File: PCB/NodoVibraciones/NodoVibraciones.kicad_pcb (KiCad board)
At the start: 2 copper layers, 17 parts, among them J1 batería, J2 UART, J3 MPU6050, SW1 SW_Push, SW2 SW_Push, SW3 SW_Nidec_CAS-120A1, U1 ESP-07, U2 MPU-6050

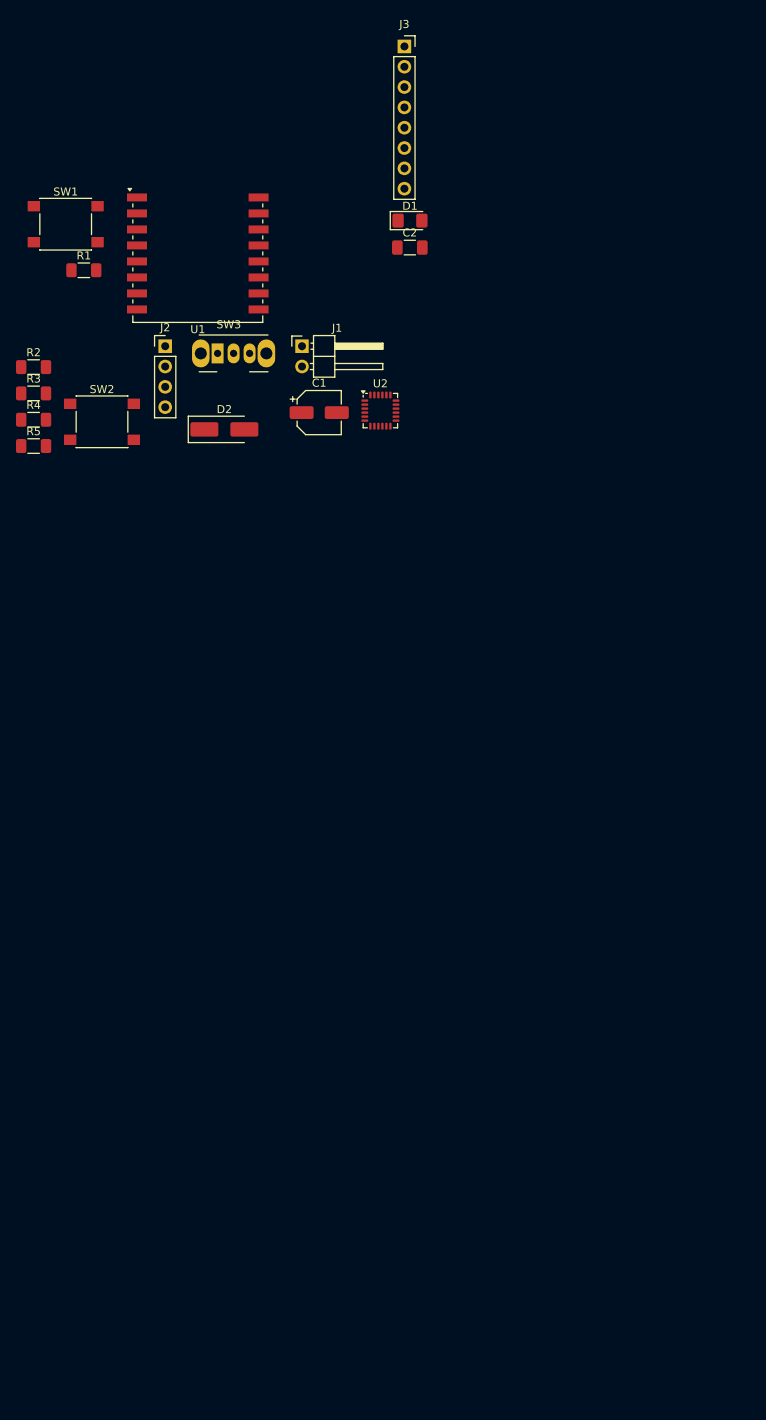
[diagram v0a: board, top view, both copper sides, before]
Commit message: Se creó PCB v0.0.1 de nodo VibraNet
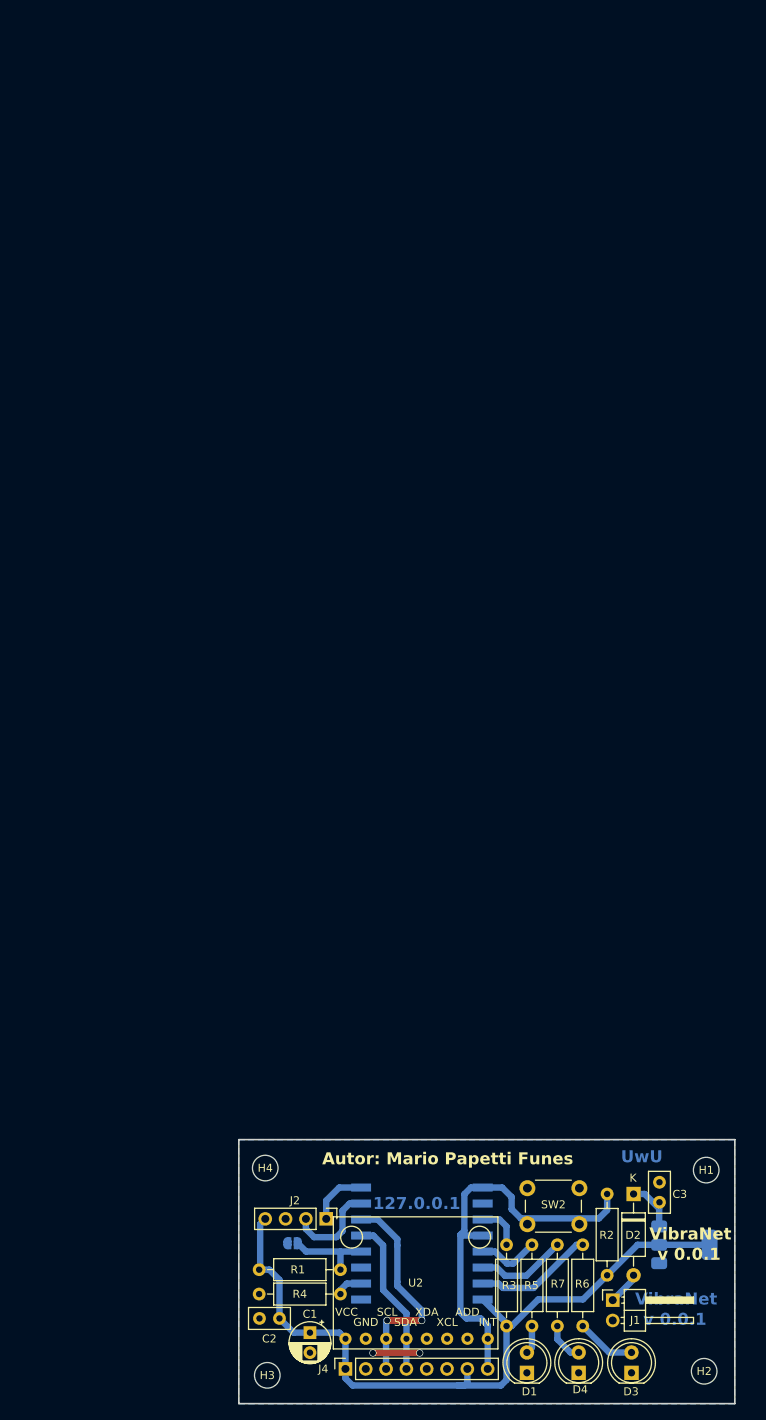
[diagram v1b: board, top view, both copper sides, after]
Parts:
- removed J3: MPU6050, Connector_PinSocket_2.54mm:PinSocket_1x08_P2.54mm_Vertical
- removed SW1: SW_Push, Button_Switch_SMD:SW_SPST_PTS645
- removed SW3: SW_Nidec_CAS-120A1, Button_Switch_THT:SW_Slide_SPDT_Angled_CK_OS102011MA1Q
- added C3: 102, Capacitor_THT:C_Disc_D5.0mm_W2.5mm_P2.50mm, F.Cu at (156.2, 216.9)
- added D3: LED, LED_THT:LED_D5.0mm, F.Cu at (152.7, 238.2)
- added D4: LED, LED_THT:LED_D5.0mm, F.Cu at (146.1, 238.2)
- added H1: MountingHole, MountingHole:MountingHole_3.2mm_M3, F.Cu at (162.1, 212.9)
- added H2: MountingHole, MountingHole:MountingHole_3.2mm_M3, F.Cu at (161.8, 238.0)
- added H3: MountingHole, MountingHole:MountingHole_3.2mm_M3, F.Cu at (107.2, 238.5)
- added H4: MountingHole, MountingHole:MountingHole_3.2mm_M3, F.Cu at (106.9, 212.6)
- added J4: MPU6050, Connector_PinSocket_2.54mm:PinSocket_1x08_P2.54mm_Vertical, F.Cu at (117.0, 237.7)
- added JP1: Jumper_2_Open, Jumper:SolderJumper-2_P1.3mm_Open_RoundedPad1.0x1.5mm, B.Cu at (110.4, 222.0)
- added R6: 1k, Resistor_THT:R_Axial_DIN0207_L6.3mm_D2.5mm_P10.16mm_Horizontal, F.Cu at (146.6, 232.4)
- added R7: 1k, Resistor_THT:R_Axial_DIN0207_L6.3mm_D2.5mm_P10.16mm_Horizontal, F.Cu at (143.4, 232.4)
- added U3: AMS1117-3.3, Package_TO_SOT_SMD:SOT-223-3_TabPin2, B.Cu at (159.3, 222.2)
- C1: footprint Capacitor_SMD:CP_Elec_5x5.4 -> Capacitor_THT:CP_Radial_D5.0mm_P2.50mm
- C2: footprint Capacitor_SMD:C_1206_3216Metric_Pad1.33x1.80mm_HandSolder -> Capacitor_THT:C_Disc_D5.0mm_W2.5mm_P2.50mm
- D1: footprint LED_SMD:LED_1206_3216Metric_Pad1.42x1.75mm_HandSolder -> LED_THT:LED_D5.0mm
- D2: footprint Diode_SMD:D_SMA_Handsoldering -> Diode_THT:D_A-405_P10.16mm_Horizontal
- R1, R2, R3, R4, R5: footprint Resistor_SMD:R_1206_3216Metric_Pad1.30x1.75mm_HandSolder -> Resistor_THT:R_Axial_DIN0207_L6.3mm_D2.5mm_P10.16mm_Horizontal
- SW2: footprint Button_Switch_SMD:SW_SPST_PTS645 -> Button_Switch_THT:SW_PUSH_6mm_H4.3mm
- U1: moved to B.Cu
- U2: value MPU-6050 -> module_mpu6050; footprint Sensor_Motion:InvenSense_QFN-24_4x4mm_P0.5mm -> USINI_sensors:module_mpu6050
- moved D1 144.8 mm to (139.6, 238.2), turned to 90 degrees
- moved C2 134.8 mm to (108.7, 231.4), turned to 180 degrees
- moved R1 129.0 mm to (116.3, 225.3), turned to 180 degrees
- moved U1 126.9 mm to (126.5, 220.0), turned to 180 degrees
- moved R5 126.4 mm to (140.3, 232.4), turned to 90 degrees
- moved R2 125.8 mm to (149.7, 215.9), turned to -90 degrees
- moved J1 125.4 mm to (150.4, 229.1)
- moved R3 121.7 mm to (137.1, 222.2), turned to -90 degrees
- moved U2 116.8 mm to (134.8, 234.0), turned to 90 degrees
- moved SW2 116.7 mm to (146.2, 219.6), turned to 180 degrees
- moved C1 115.0 mm to (112.5, 233.2), turned to -90 degrees
- moved R4 112.9 mm to (106.2, 228.4)
- moved J2 110.9 mm to (114.6, 219.0), turned to -90 degrees
- moved D2 108.4 mm to (153.0, 215.9), turned to -90 degrees
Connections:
- net Net-(U1-EN) renamed /EN
- net Net-(U1-GPIO0) renamed boot
- net Net-(U1-GPIO15) renamed /magic
- D2 pad 1: VCC -> /Vin
- D2 pad 2: Net-(D2-A) -> /Vbat
- J1 pad 1: Net-(J1-Pin_1) -> /Vbat
- R2 pad 1: Net-(U1-~{RST}) -> int1
- R5 pad 2: Net-(U1-GPIO13) -> /led-aux
- SW2 pad 1: Net-(U1-~{RST}) -> int1
- U1 pad 1: Net-(U1-~{RST}) -> int1
- U1 pad 4: unconnected-(U1-GPIO16-Pad4) -> int1
- U1 pad 5: unconnected-(U1-GPIO14-Pad5) -> /led-aux
- U1 pad 6: unconnected-(U1-GPIO12-Pad6) -> /led-wifi
- U1 pad 7: Net-(U1-GPIO13) -> /led-data
- U2 pad 1: unconnected-(U2-CLKIN-Pad1) -> VCC
- U2 pad 2: unconnected-(U2-NC-Pad2) -> GNDREF
- U2 pad 3: unconnected-(U2-NC-Pad3) -> SCL
- U2 pad 4: unconnected-(U2-NC-Pad4) -> SDA
- U2 pad 7: unconnected-(U2-AUX_CL-Pad7) -> GNDREF
- U2 pad 8: unconnected-(U2-VLOGIC-Pad8) -> int1
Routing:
- net VCC: track 0.00 -> 93.5 mm
- net int1: track 0.00 -> 50.5 mm
- net SCL: track 0.00 -> 27.5 mm, vias 0 -> 2
- net SDA: track 0.00 -> 19.9 mm
- net /led-data: track 0.00 -> 15.0 mm
- net RX: track 0.00 -> 11.8 mm
- net /led-wifi: track 0.00 -> 11.4 mm
- net boot: track 0.00 -> 10.6 mm
- net /led-aux: track 0.00 -> 7.75 mm
- net Net-(D3-A): track 0.00 -> 7.46 mm
- net TX: track 0.00 -> 7.32 mm
- net /Vin: track 0.00 -> 6.20 mm
- net GNDREF: track 0.00 -> 5.84 mm, vias 0 -> 2
- net /EN: track 0.00 -> 5.63 mm
- net Net-(D4-A): track 0.00 -> 5.00 mm
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- added copper zone on B.Cu, net GNDREF
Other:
- board outline added: 62 x 33 mm
- board text added: "127.0.0.1"
- board text added: "Autor: Mario Papetti Funes"
- board text added: "UwU"
- board text added: "VibraNet"
- board text added: "v 0.0.1"

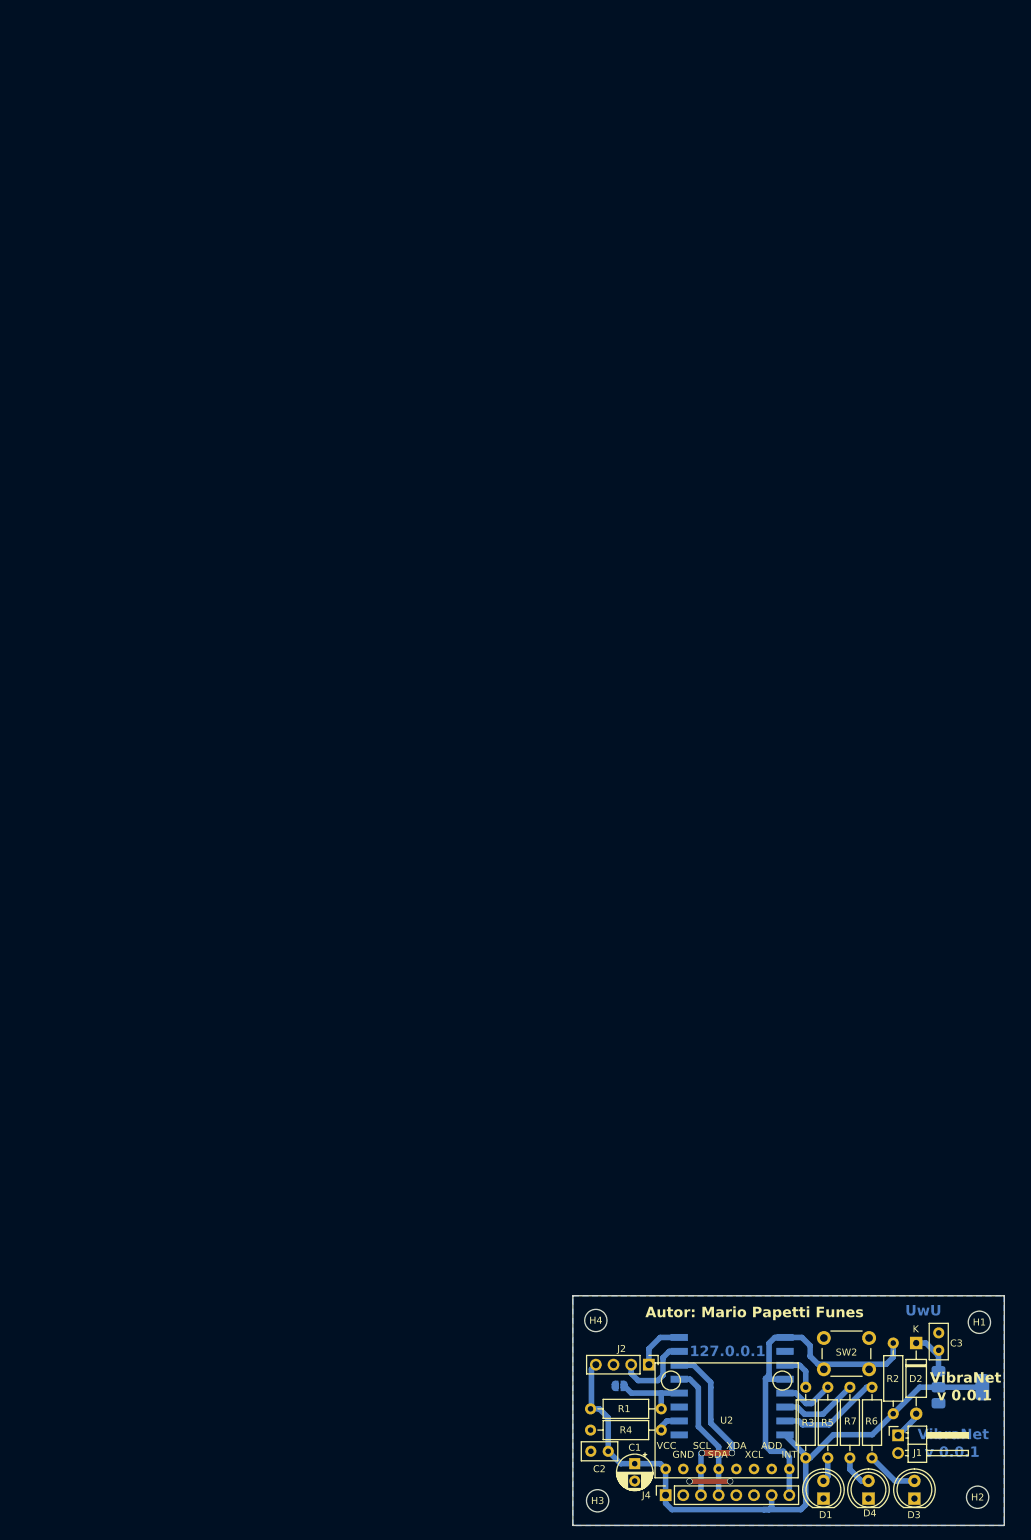
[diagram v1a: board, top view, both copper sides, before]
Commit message: se agregó la carpeta node-red para trabajar con los flujos de node-red
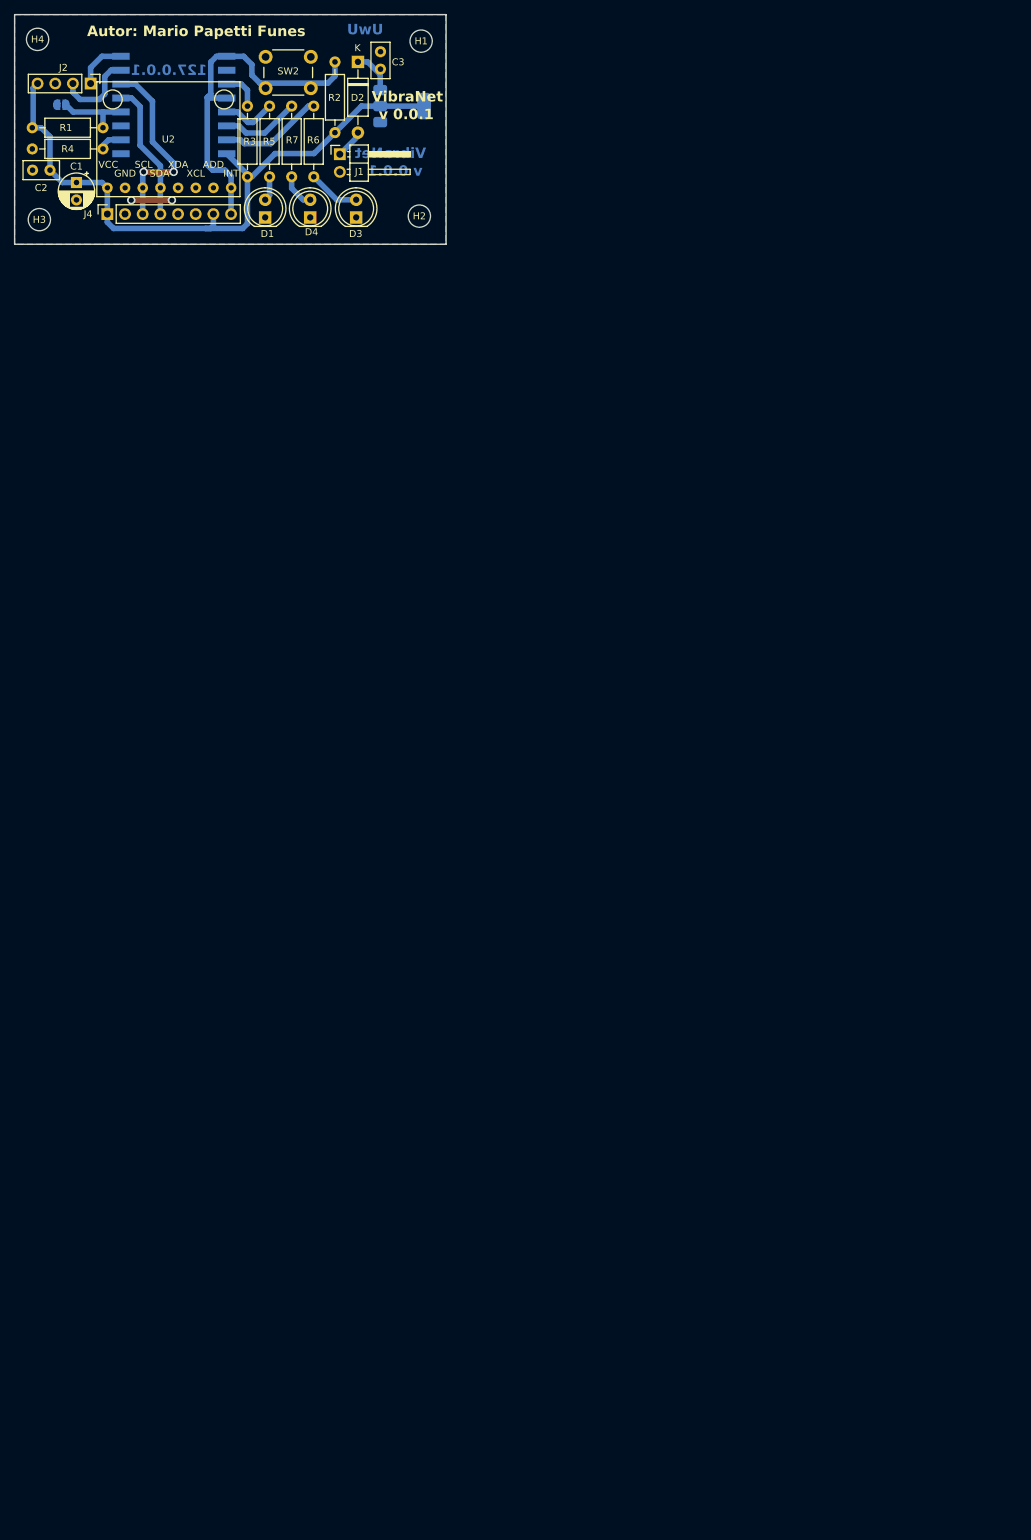
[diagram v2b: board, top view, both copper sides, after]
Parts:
- moved C1 200.8 mm to (32.3, 49.1)
- moved C2 200.8 mm to (28.5, 47.3)
- moved C3 200.8 mm to (76.0, 32.8)
- moved D1 200.8 mm to (59.4, 54.1)
- moved D3 200.8 mm to (72.5, 54.1)
- moved D4 200.8 mm to (65.9, 54.1)
- moved H1 200.8 mm to (81.8, 28.8)
- moved H3 200.8 mm to (27.0, 54.4)
- moved J1 200.8 mm to (70.1, 45.0)
- moved R1 200.8 mm to (36.1, 41.2)
- moved R4 200.8 mm to (25.9, 44.3)
- moved SW2 200.8 mm to (66.0, 35.5)
- moved U1 200.8 mm to (46.3, 35.9)
- moved U2 200.8 mm to (54.5, 49.9)
- moved D2 200.8 mm to (72.7, 31.8)
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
